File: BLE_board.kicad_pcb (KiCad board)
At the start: 4 copper layers, 53.9 x 29.1 mm, 51 parts, among them J1 USB_C_Receptacle_USB2.0_14P, J2 SWD, SW1 NRST, SW2 BOOT0, U1 STM32F042G6U6, U2 nRF24L01P, U3 USBLC6-2P6, U5 MIC5365-3.3YC5, Y1 16MHz

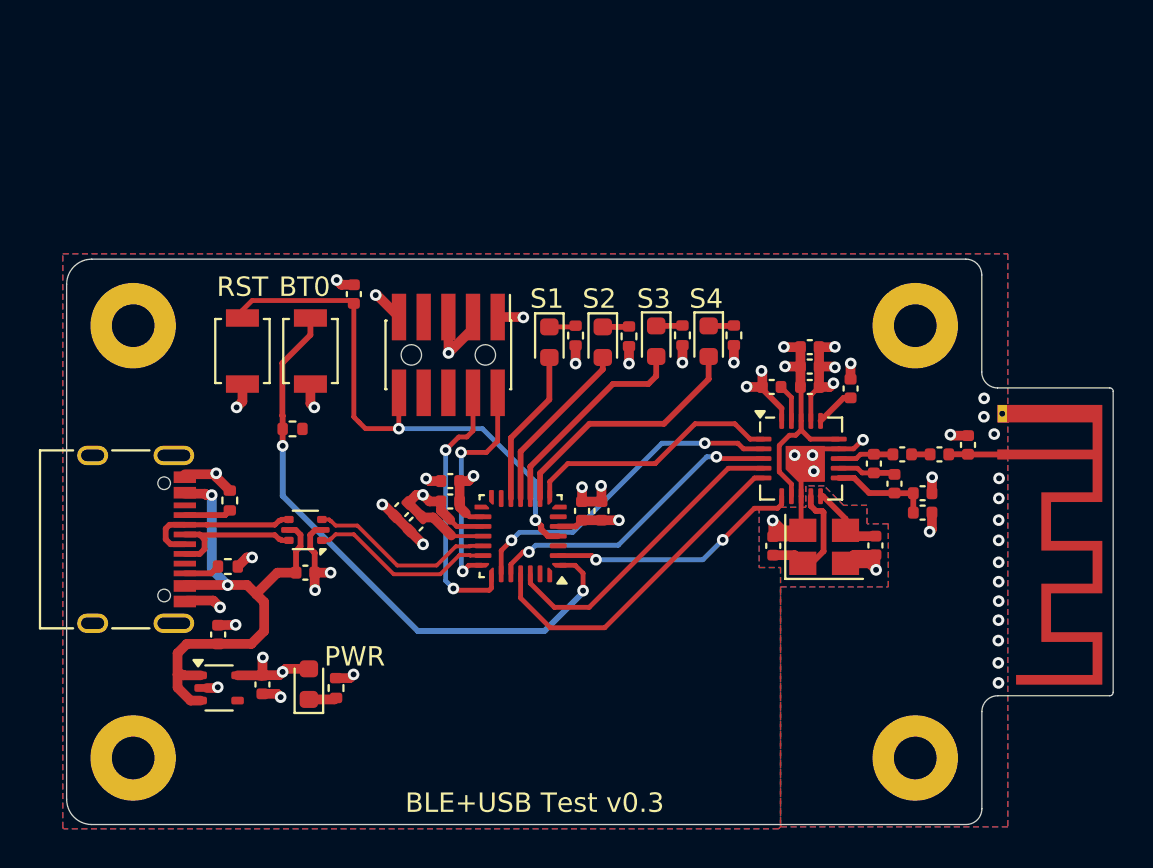
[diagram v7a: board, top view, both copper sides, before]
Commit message: Migrated the STM32F0 to an STM32G0B
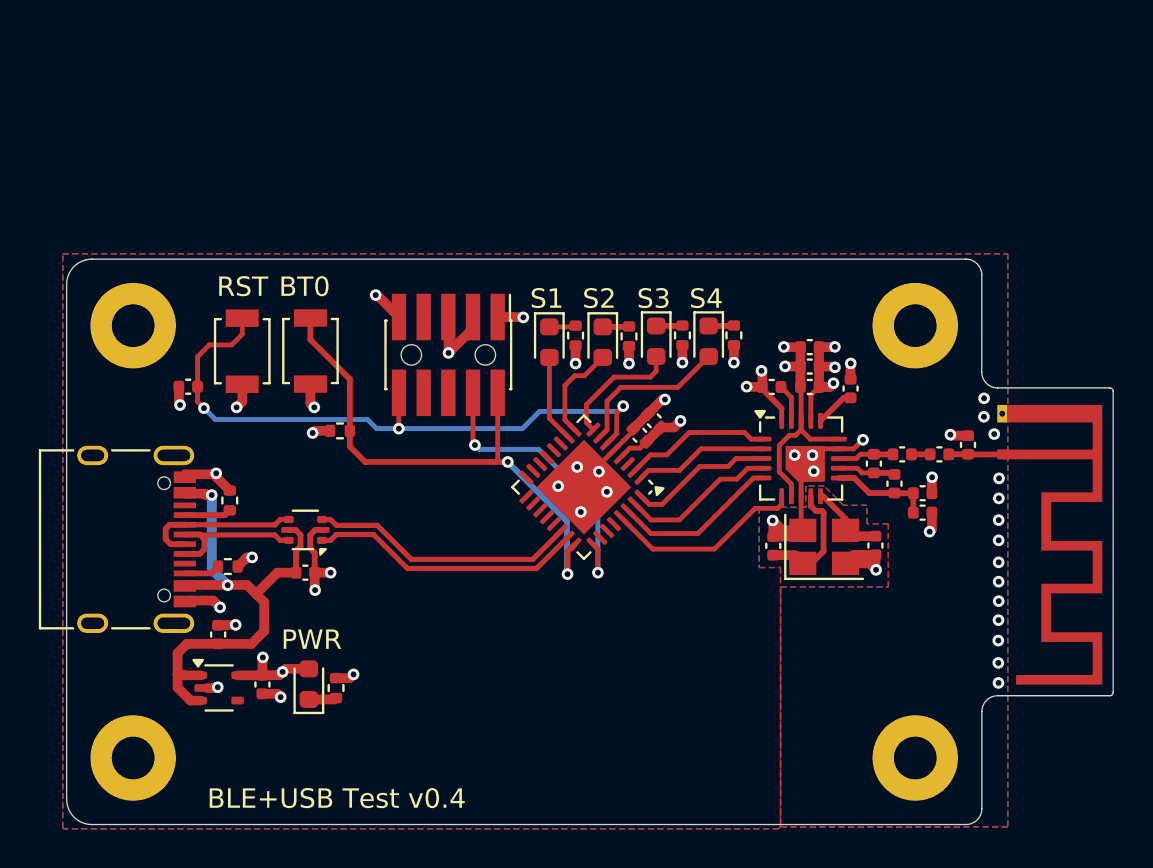
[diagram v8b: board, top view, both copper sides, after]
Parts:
- removed C13: 4.7u, Capacitor_SMD:C_0402_1005Metric
- removed C14: 100n, Capacitor_SMD:C_0402_1005Metric
- removed C15: 1u, Capacitor_SMD:C_0402_1005Metric
- removed C16: 10n, Capacitor_SMD:C_0402_1005Metric
- removed U1: STM32F042G6U6, Package_DFN_QFN:QFN-28_4x4mm_P0.5mm
- added U301: STM32G0B1KEU6, Package_DFN_QFN:QFN-32-1EP_5x5mm_P0.5mm_EP3.45x3.45mm, F.Cu at (117.1, 77.0)
- moved C2 11.3 mm to (120.8, 73.6), turned to 135 degrees
- moved C1 10.0 mm to (120.0, 74.3), turned to 135 degrees
- moved C21 9.77 mm to (96.8, 71.8), turned to 180 degrees
- moved R4 2.44 mm to (104.6, 74.1), turned to 0 degrees
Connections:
- J2 pad 2: /MCU Module/SWDIO -> /MCU Module/SWDIO/BOOT0
- R4 pad 2: /MCU Module/boot0 -> /MCU Module/SWDIO/BOOT0
- SW2 pad 1: /MCU Module/boot0 -> /MCU Module/SWDIO/BOOT0
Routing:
- net /MCU Module/boot0: track 31.3 -> 0.00 mm, vias 2 -> 0
- net /MCU Module/SWDIO/BOOT0: track 0.00 -> 28.2 mm, vias 0 -> 2
- net /MCU Module/SWDIO: track 11.9 -> 0.00 mm, vias 2 -> 0
- net /MCU Module/SPI_CS: track 17.1 -> 6.91 mm, vias 2 -> 0
- net +3V3: track 33.7 -> 23.8 mm, vias 9 -> 7
- net /MCU Module/SPI_MISO: track 17.6 -> 8.67 mm
- net /MCU Module/SPI_SCK: track 15.8 -> 7.42 mm, vias 2 -> 0
- net /MCU Module/SPI_MOSI: track 16.0 -> 8.09 mm
- net /MCU Module/RF_CE: track 13.4 -> 7.59 mm
- net /MCU Module/SIG4: track 13.2 -> 8.14 mm
- net /MCU Module/NRST: track 28.5 -> 33.2 mm, vias 2 -> 3
- net /MCU Module/SIG3: track 11.1 -> 6.50 mm
- net /MCU Module/USB_D+: track 9.69 -> 14.2 mm
- net /MCU Module/USB_D-: track 9.69 -> 13.8 mm
- net /MCU Module/SIG2: track 9.01 -> 5.02 mm
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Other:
- board text added: "BLE+USB Test v0.4"
- board text removed: "BLE+USB Test v0.3"
